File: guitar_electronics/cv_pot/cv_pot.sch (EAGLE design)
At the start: 8 parts

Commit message: push Nexus peripheral files
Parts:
- removed R1: 20K, resistor:R-EU_R0402
- removed SJ1: (no value), jumper:SJ
- added C3: 1uF, resistor:C-EUC0603
- added U1: L78LXX, CYCFI_Power:L78LXX
- C1: device resistor:C-EUC0603 -> resistor:C-EUC0402
- C2: device resistor:C-EUC0805 -> resistor:C-EUC0603
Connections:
- net GND: now also C2.1, C3.1, U1.GND, U1.GND1; no longer C2.2
- net N$1: now also C2.2, U1.OUT; no longer C2.1, R1.2, SJ1.2
- net N$2: now also C3.2, U1.IN; no longer R1.1, SJ1.1
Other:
- note added: "CJ75L05"
- note added: "CV_Pot for Nexus Project by Cycfi Research is licensed under a Creative Commons Attribution-ShareAlike 4.0 International License. Copyright CYCFI Research Inc. 2013-2020"
- note added: "VCC"
- note added: "v2.5"
- note removed: "2017030"
- note removed: "CV_Pot for Nexus Project by Cycfi Research is licensed under a Creative Commons Attribution-ShareAlike 4.0 International License. Copyright CYCFI Research Inc. 2013-2017"
- note removed: "VCC(9V)"
- note removed: "v0.96"
- moved on the sheet: C1, C2, H1, POT1

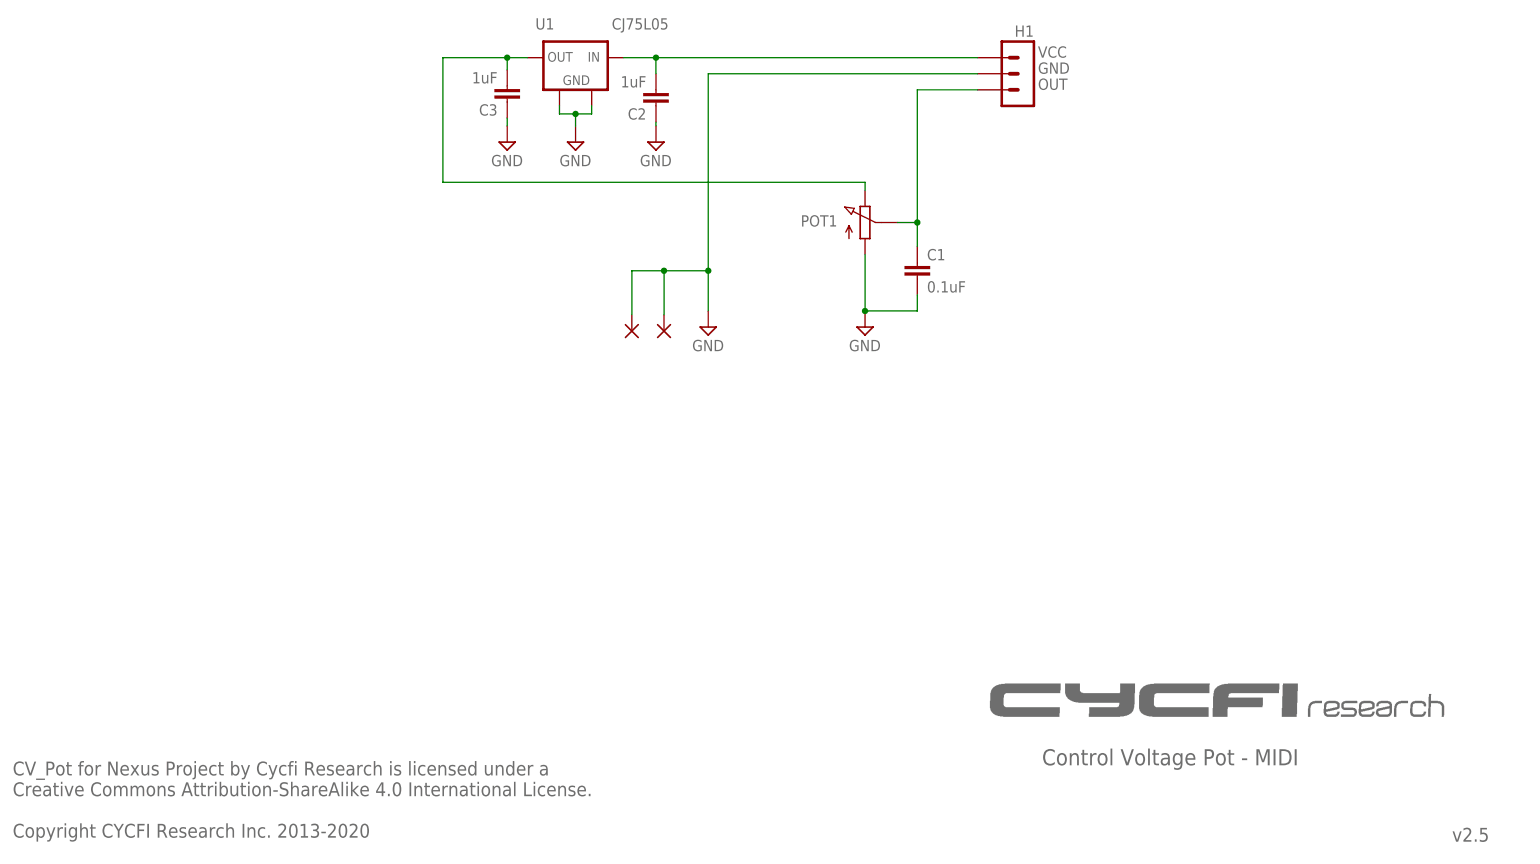
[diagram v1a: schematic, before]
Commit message: updated schematic and bom files for cv pot
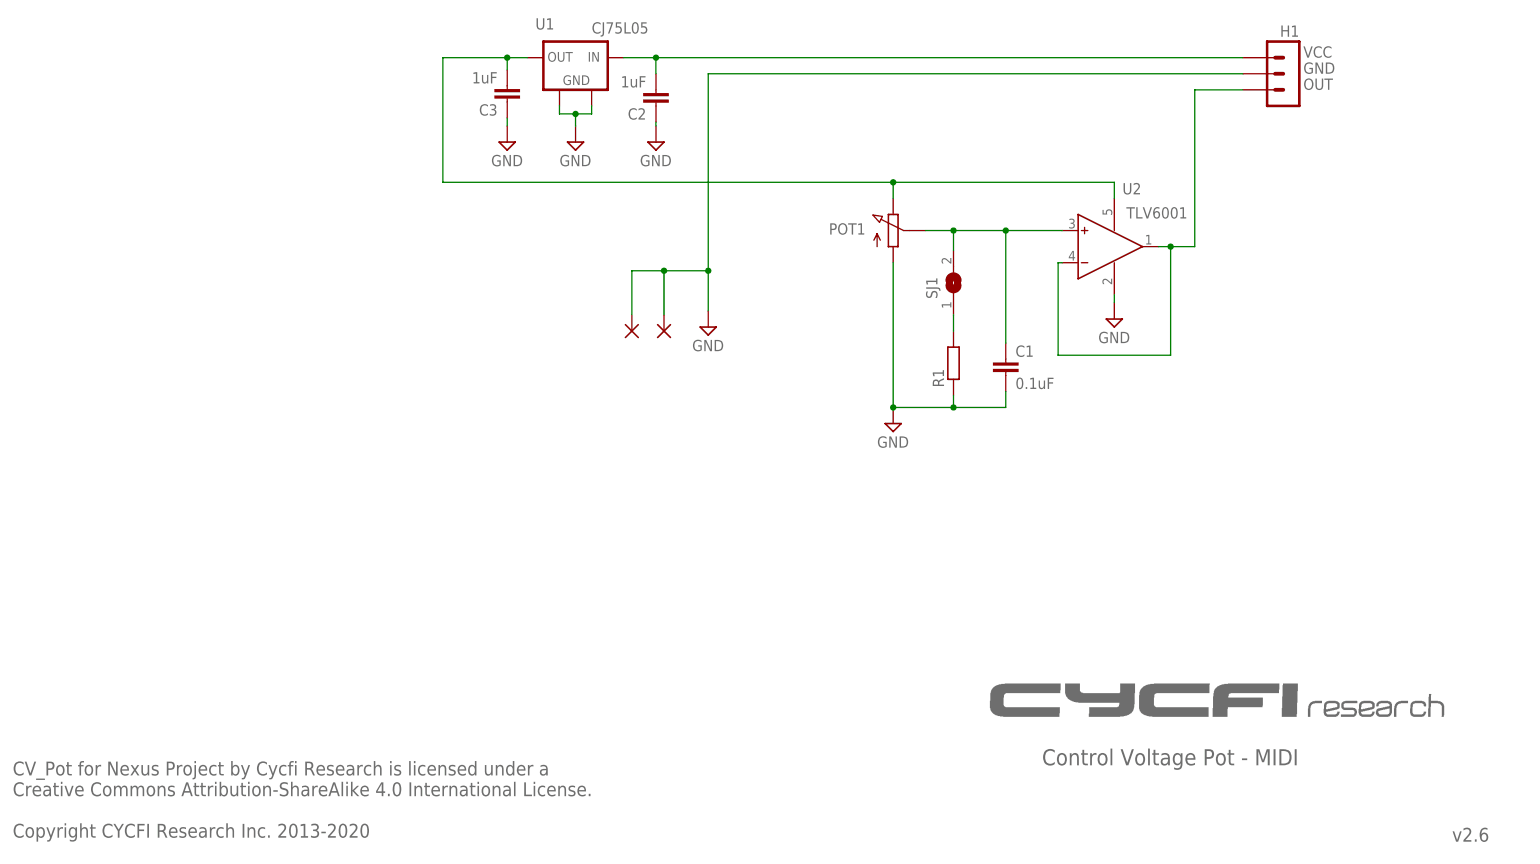
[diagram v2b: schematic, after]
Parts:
- added R1: (no value), rcl:R-EU_R0402
- added SJ1: (no value), jumper:SJ
- added U2: TLV6001, CYCFI_semicon:TLV170
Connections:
- removed net OUT: C1.1, H1.1, POT1.2
- new net N$3: C1.1, POT1.2, SJ1.2, U2G$1.IN+
- new net N$4: R1.2, SJ1.1
- new net N$5: H1.1, U2G$1.IN-, U2G$1.OUT
- net GND: now also R1.1, U2G$2.V-
- net N$2: now also U2G$2.V+
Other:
- note added: "U2"
- note added: "v2.6"
- note removed: "v2.5"
- moved on the sheet: C1, H1, POT1
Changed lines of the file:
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@@
 <setting verticaltext="up"/>
 </settings>
-<grid distance="0.025" unitdist="inch" unit="inch" style="lines" multiple="1" display="yes" altdistance="0.01" altunitdist="inch" altunit="inch"/>
+<grid distance="0.1" unitdist="inch" unit="inch" style="lines" multiple="1" display="no" altdistance="0.01" altunitdist="inch" altunit="inch"/>
 <layers>
 <layer number="1" name="Top" color="4" fill="1" visible="no" active="no"/>
@@
 <part name="SUPPLY2" library="supply2" deviceset="GND" device=""/>
 <part name="SUPPLY3" library="supply2" deviceset="GND" device=""/>
+<part name="R1" library="rcl" deviceset="R-EU_" device="R0402"/>
+<part name="SJ1" library="jumper" deviceset="SJ" device=""/>
+<part name="SUPPLY4" library="supply2" deviceset="GND" device=""/>
+<part name="U2" library="CYCFI_semicon" deviceset="TLV170" device="" value="TLV6001"/>
 </parts>
 <sheets>
@@
 <plain>
 <text x="172.72" y="19.05" size="2.54" layer="95" font="vector">Control Voltage Pot - MIDI</text>
-<text x="172.085" y="130.81" size="1.778" layer="95">VCC</text>
-<text x="172.085" y="128.27" size="1.778" layer="95">GND</text>
-<text x="172.085" y="125.73" size="1.778" layer="95">OUT</text>
-<text x="237.49" y="6.985" size="2.1844" layer="95" font="vector">v2.5</text>
+<text x="213.995" y="130.81" size="1.778" layer="95">VCC</text>
+<text x="213.995" y="128.27" size="1.778" layer="95">GND</text>
+<text x="213.995" y="125.73" size="1.778" layer="95">OUT</text>
+<text x="237.49" y="6.985" size="2.1844" layer="95" font="vector">v2.6</text>
 <text x="10.16" y="7.62" size="2.1844" layer="95" font="vector">CV_Pot for Nexus Project by Cycfi Research is licensed under a
 Creative Commons Attribution-ShareAlike 4.0 International License.
@@
 <rectangle x1="202.08875" y1="31.90875" x2="210.21675" y2="31.97225" layer="95"/>
 <rectangle x1="210.78825" y1="31.90875" x2="213.13775" y2="31.97225" layer="95"/>
-<text x="104.775" y="135.255" size="1.778" layer="95">CJ75L05</text>
+<text x="101.6" y="134.62" size="1.778" layer="95">CJ75L05</text>
+<text x="185.42" y="109.22" size="1.778" layer="95">U2</text>
 </plain>
 <instances>
@@
 <attribute name="VALUE" x="116.332" y="86.487" size="1.778" layer="96" rot="R90"/>
 </instance>
-<instance part="POT1" gate="G$1" x="144.78" y="104.775" smashed="yes">
-<attribute name="NAME" x="134.62" y="104.14" size="1.778" layer="95"/>
+<instance part="POT1" gate="G$1" x="149.225" y="103.505" smashed="yes">
+<attribute name="NAME" x="139.065" y="102.87" size="1.778" layer="95"/>
 </instance>
 <instance part="SUPPLY16" gate="GND" x="120.015" y="88.265" smashed="yes">
 <attribute name="VALUE" x="117.475" y="84.455" size="1.778" layer="96"/>
 </instance>
-<instance part="H1" gate="G$1" x="170.18" y="128.27" smashed="yes" rot="MR0">
-<attribute name="NAME" x="171.45" y="134.112" size="1.778" layer="95" rot="MR0"/>
+<instance part="H1" gate="G$1" x="212.09" y="128.27" smashed="yes" rot="MR0">
+<attribute name="NAME" x="213.36" y="134.112" size="1.778" layer="95" rot="MR0"/>
 </instance>
-<instance part="SUPPLY10" gate="GND" x="144.78" y="88.265" smashed="yes">
-<attribute name="VALUE" x="142.24" y="84.455" size="1.778" layer="96"/>
+<instance part="SUPPLY10" gate="GND" x="149.225" y="73.025" smashed="yes">
+<attribute name="VALUE" x="146.685" y="69.215" size="1.778" layer="96"/>
 </instance>
 <instance part="U1" gate="G$1" x="99.06" y="128.27" smashed="yes">
@@
 <attribute name="VALUE" x="96.52" y="113.665" size="1.778" layer="96"/>
 </instance>
-<instance part="C1" gate="G$1" x="153.035" y="98.425"/>
+<instance part="C1" gate="G$1" x="167.005" y="83.185"/>
 <instance part="C2" gate="G$1" x="111.76" y="123.19" rot="R180"/>
 <instance part="C3" gate="G$1" x="88.265" y="123.825" rot="R180"/>
@@
 <attribute name="VALUE" x="109.22" y="113.665" size="1.778" layer="96"/>
 </instance>
+<instance part="R1" gate="G$1" x="158.75" y="82.55" rot="R90"/>
+<instance part="SJ1" gate="1" x="158.75" y="95.25" rot="R90"/>
+<instance part="SUPPLY4" gate="GND" x="184.15" y="89.535" smashed="yes">
+<attribute name="VALUE" x="181.61" y="85.725" size="1.778" layer="96"/>
+</instance>
+<instance part="U2" gate="G$1" x="180.975" y="100.965" smashed="yes">
+<attribute name="VALUE" x="186.055" y="105.41" size="1.778" layer="96"/>
+</instance>
+<instance part="U2" gate="G$2" x="184.15" y="100.965" smashed="yes"/>
 </instances>
 <busses>
@@
 <segment>
 <pinref part="H1" gate="G$1" pin="3"/>
-<wire x1="162.56" y1="130.81" x2="111.76" y2="130.81" width="0.1524" layer="91"/>
+<wire x1="204.47" y1="130.81" x2="111.76" y2="130.81" width="0.1524" layer="91"/>
 <pinref part="U1" gate="G$1" pin="OUT"/>
 <pinref part="C2" gate="G$1" pin="2"/>
@@
 <pinref part="POT1" gate="G$1" pin="1"/>
 <pinref part="SUPPLY10" gate="GND" pin="GND"/>
-<wire x1="144.78" y1="99.695" x2="144.78" y2="90.805" width="0.1524" layer="91"/>
-<wire x1="153.035" y1="93.345" x2="153.035" y2="90.805" width="0.1524" layer="91"/>
-<wire x1="153.035" y1="90.805" x2="144.78" y2="90.805" width="0.1524" layer="91"/>
-<junction x="144.78" y="90.805"/>
+<wire x1="149.225" y1="98.425" x2="149.225" y2="75.565" width="0.1524" layer="91"/>
+<wire x1="167.005" y1="78.105" x2="167.005" y2="75.565" width="0.1524" layer="91"/>
+<wire x1="167.005" y1="75.565" x2="158.75" y2="75.565" width="0.1524" layer="91"/>
+<junction x="149.225" y="75.565"/>
 <pinref part="C1" gate="G$1" pin="2"/>
+<pinref part="R1" gate="G$1" pin="1"/>
+<wire x1="158.75" y1="75.565" x2="149.225" y2="75.565" width="0.1524" layer="91"/>
+<wire x1="158.75" y1="77.47" x2="158.75" y2="75.565" width="0.1524" layer="91"/>
+<junction x="158.75" y="75.565"/>
 </segment>
 <segment>
@@
 <junction x="113.03" y="97.155"/>
 <junction x="120.015" y="97.155"/>
-<wire x1="162.56" y1="128.27" x2="120.015" y2="128.27" width="0.1524" layer="91"/>
+<wire x1="204.47" y1="128.27" x2="120.015" y2="128.27" width="0.1524" layer="91"/>
 </segment>
 <segment>
@@
 <wire x1="88.265" y1="120.015" x2="88.265" y2="121.285" width="0.1524" layer="91"/>
 </segment>
-</net>
-<net name="OUT" class="0">
 <segment>
-<pinref part="POT1" gate="G$1" pin="2"/>
-<wire x1="149.86" y1="104.775" x2="153.035" y2="104.775" width="0.1524" layer="91"/>
-<wire x1="153.035" y1="104.775" x2="153.035" y2="100.965" width="0.1524" layer="91"/>
-<pinref part="H1" gate="G$1" pin="1"/>
-<wire x1="153.035" y1="104.775" x2="153.035" y2="125.73" width="0.1524" layer="91"/>
-<wire x1="153.035" y1="125.73" x2="162.56" y2="125.73" width="0.1524" layer="91"/>
-<junction x="153.035" y="104.775"/>
-<pinref part="C1" gate="G$1" pin="1"/>
+<pinref part="SUPPLY4" gate="GND" pin="GND"/>
+<wire x1="184.15" y1="92.075" x2="184.15" y2="93.345" width="0.1524" layer="91"/>
+<pinref part="U2" gate="G$2" pin="V-"/>
 </segment>
 </net>
@@
 <pinref part="U1" gate="G$1" pin="IN"/>
 <wire x1="88.265" y1="130.81" x2="91.44" y2="130.81" width="0.1524" layer="91"/>
-<pinref part="POT1" gate="G$1" pin="3"/>
-<wire x1="144.78" y1="109.855" x2="144.78" y2="111.125" width="0.1524" layer="91"/>
-<wire x1="144.78" y1="111.125" x2="78.105" y2="111.125" width="0.1524" layer="91"/>
 <wire x1="78.105" y1="111.125" x2="78.105" y2="130.81" width="0.1524" layer="91"/>
 <wire x1="78.105" y1="130.81" x2="88.265" y2="130.81" width="0.1524" layer="91"/>
 <junction x="88.265" y="130.81"/>
+<pinref part="POT1" gate="G$1" pin="3"/>
+<wire x1="78.105" y1="111.125" x2="149.225" y2="111.125" width="0.1524" layer="91"/>
+<wire x1="149.225" y1="111.125" x2="149.225" y2="108.585" width="0.1524" layer="91"/>
+<wire x1="184.15" y1="108.585" x2="184.15" y2="111.125" width="0.1524" layer="91"/>
+<wire x1="184.15" y1="111.125" x2="149.225" y2="111.125" width="0.1524" layer="91"/>
+<junction x="149.225" y="111.125"/>
+<pinref part="U2" gate="G$2" pin="V+"/>
 </segment>
 </net>
+<net name="N$3" class="0">
+<segment>
+<pinref part="C1" gate="G$1" pin="1"/>
+<pinref part="POT1" gate="G$1" pin="2"/>
+<wire x1="167.005" y1="85.725" x2="167.005" y2="103.505" width="0.1524" layer="91"/>
+<wire x1="167.005" y1="103.505" x2="158.75" y2="103.505" width="0.1524" layer="91"/>
+<pinref part="SJ1" gate="1" pin="2"/>
+<wire x1="158.75" y1="103.505" x2="154.305" y2="103.505" width="0.1524" layer="91"/>
+<wire x1="158.75" y1="100.33" x2="158.75" y2="103.505" width="0.1524" layer="91"/>
+<junction x="158.75" y="103.505"/>
+<wire x1="175.895" y1="103.505" x2="167.005" y2="103.505" width="0.1524" layer="91"/>
+<junction x="167.005" y="103.505"/>
+<pinref part="U2" gate="G$1" pin="IN+"/>
+</segment>
+</net>
+<net name="N$4" class="0">
+<segment>
+<pinref part="SJ1" gate="1" pin="1"/>
+<pinref part="R1" gate="G$1" pin="2"/>
+<wire x1="158.75" y1="90.17" x2="158.75" y2="87.63" width="0.1524" layer="91"/>
+</segment>
+</net>
+<net name="N$5" class="0">
+<segment>
+<wire x1="175.895" y1="98.425" x2="175.26" y2="98.425" width="0.1524" layer="91"/>
+<wire x1="175.26" y1="98.425" x2="175.26" y2="83.82" width="0.1524" layer="91"/>
+<wire x1="175.26" y1="83.82" x2="193.04" y2="83.82" width="0.1524" layer="91"/>
+<wire x1="193.04" y1="83.82" x2="193.04" y2="100.965" width="0.1524" layer="91"/>
+<wire x1="193.04" y1="100.965" x2="191.135" y2="100.965" width="0.1524" layer="91"/>
+<pinref part="H1" gate="G$1" pin="1"/>
+<wire x1="204.47" y1="125.73" x2="196.85" y2="125.73" width="0.1524" layer="91"/>
+<wire x1="196.85" y1="125.73" x2="196.85" y2="100.965" width="0.1524" layer="91"/>
+<wire x1="196.85" y1="100.965" x2="193.04" y2="100.965" width="0.1524" layer="91"/>
+<junction x="193.04" y="100.965"/>
+<pinref part="U2" gate="G$1" pin="IN-"/>
+<pinref part="U2" gate="G$1" pin="OUT"/>
+</segment>
+</net>
